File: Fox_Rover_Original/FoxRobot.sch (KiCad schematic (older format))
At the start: 42 parts, among them J1 Screw_Terminal_01x02, J2 XT60-M_Green, J3 XT60-M_Red, J4 Screw_Terminal_01x02, J5 Conn_02x10_Odd_Even, J6 Screw_Terminal_01x02, J7 Conn_02x10_Odd_Even, K1 40.52.7.012.0000, K2 G2RK-1_12DC, K3 ADJH23005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

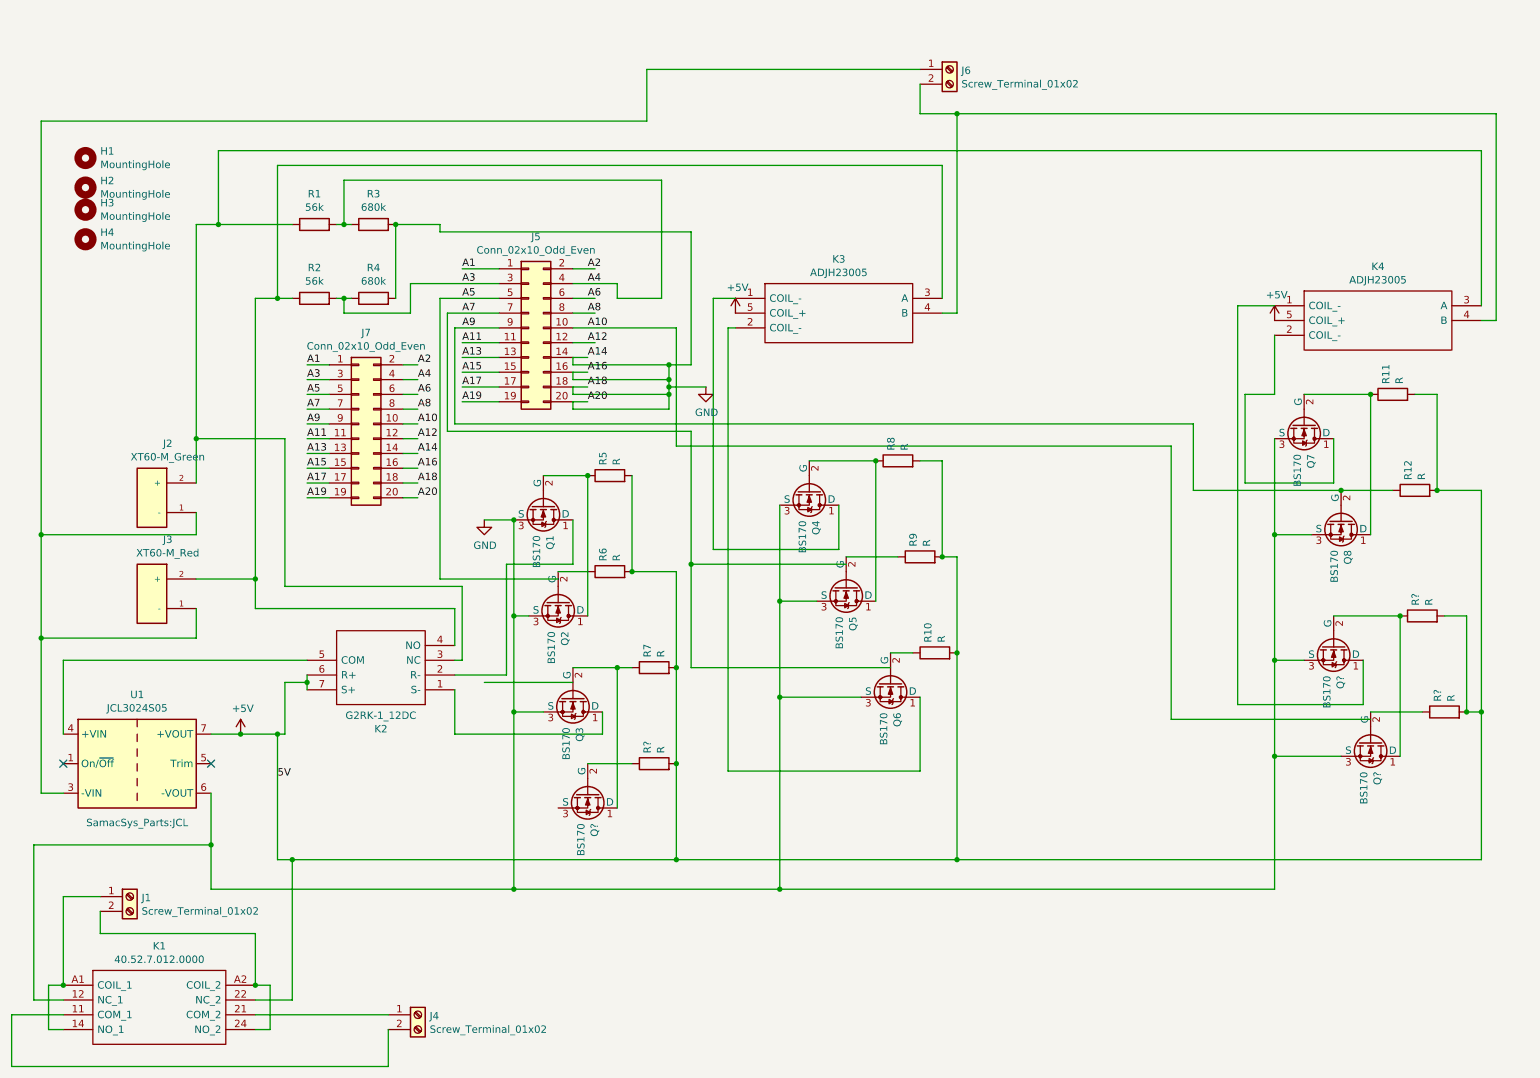
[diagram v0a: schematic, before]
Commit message: Added the filter capacitor and coil.
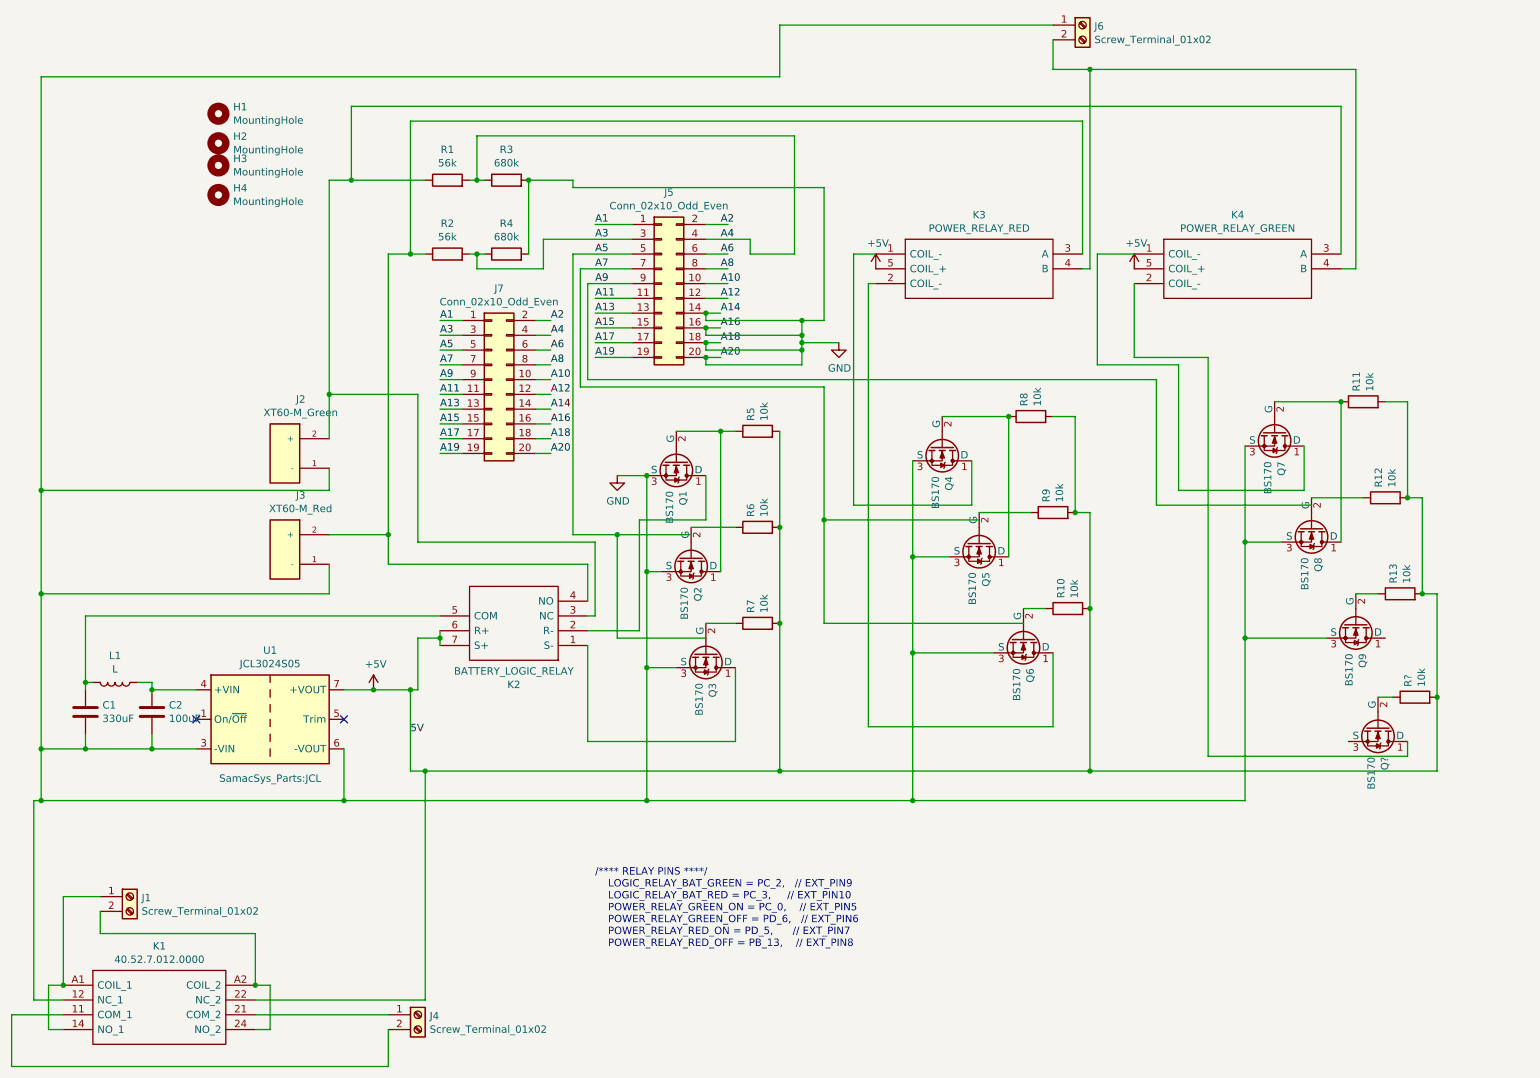
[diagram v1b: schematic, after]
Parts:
- removed Q? (x3): BS170, Package_TO_SOT_THT:TO-92_Inline, symbol Transistor_FET:BS170
- removed R? (x3): R, Resistor_THT:R_Axial_DIN0207_L6.3mm_D2.5mm_P10.16mm_Horizontal, symbol Device:R
- added C1: 330uF, Capacitor_THT:C_Disc_D7.5mm_W2.5mm_P5.00mm, symbol Device:C
- added C2: 100uF, Capacitor_THT:C_Disc_D7.5mm_W2.5mm_P5.00mm, symbol Device:C
- added L1: L, Inductor_THT:L_Radial_D10.0mm_P5.00mm_Fastron_07M, symbol Device:L
- added Q9, Q?: BS170, Package_TO_SOT_THT:TO-92_Inline, symbol Transistor_FET:BS170
- added R13, R?: 10k, Resistor_THT:R_Axial_DIN0207_L6.3mm_D2.5mm_P10.16mm_Horizontal, symbol Device:R
- K2: value G2RK-1_12DC -> BATTERY_LOGIC_RELAY
- K3: value ADJH23005 -> POWER_RELAY_RED
- K4: value ADJH23005 -> POWER_RELAY_GREEN
- R10, R11, R12, R5, R6, R7, R8, R9: value R -> 10k
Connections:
- wire segments 245 -> 247
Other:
- note added: "/**** RELAY PINS ****/\n LOGIC_RELAY_BAT_GREEN = PC_2, // EXT_PIN9\n LOGIC_RELAY_BAT_RED = PC_3, // EXT_PIN10\n POWER_RELAY_GREEN_ON = PC_0, // EXT_PIN5\n POWER_RELAY_GREEN_OFF = PD_6, // EXT_PIN6\n POWER_RELAY_RED_ON = PD_5, // EXT_PIN7\n POWER_RELAY_RED_OFF = PB_13, // EXT_PIN8"
- moved on the sheet: H1, H2, H3, H4, J2, J3, J5, J6, J7, K2, K3, K4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

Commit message: Adjusted libraries pathing
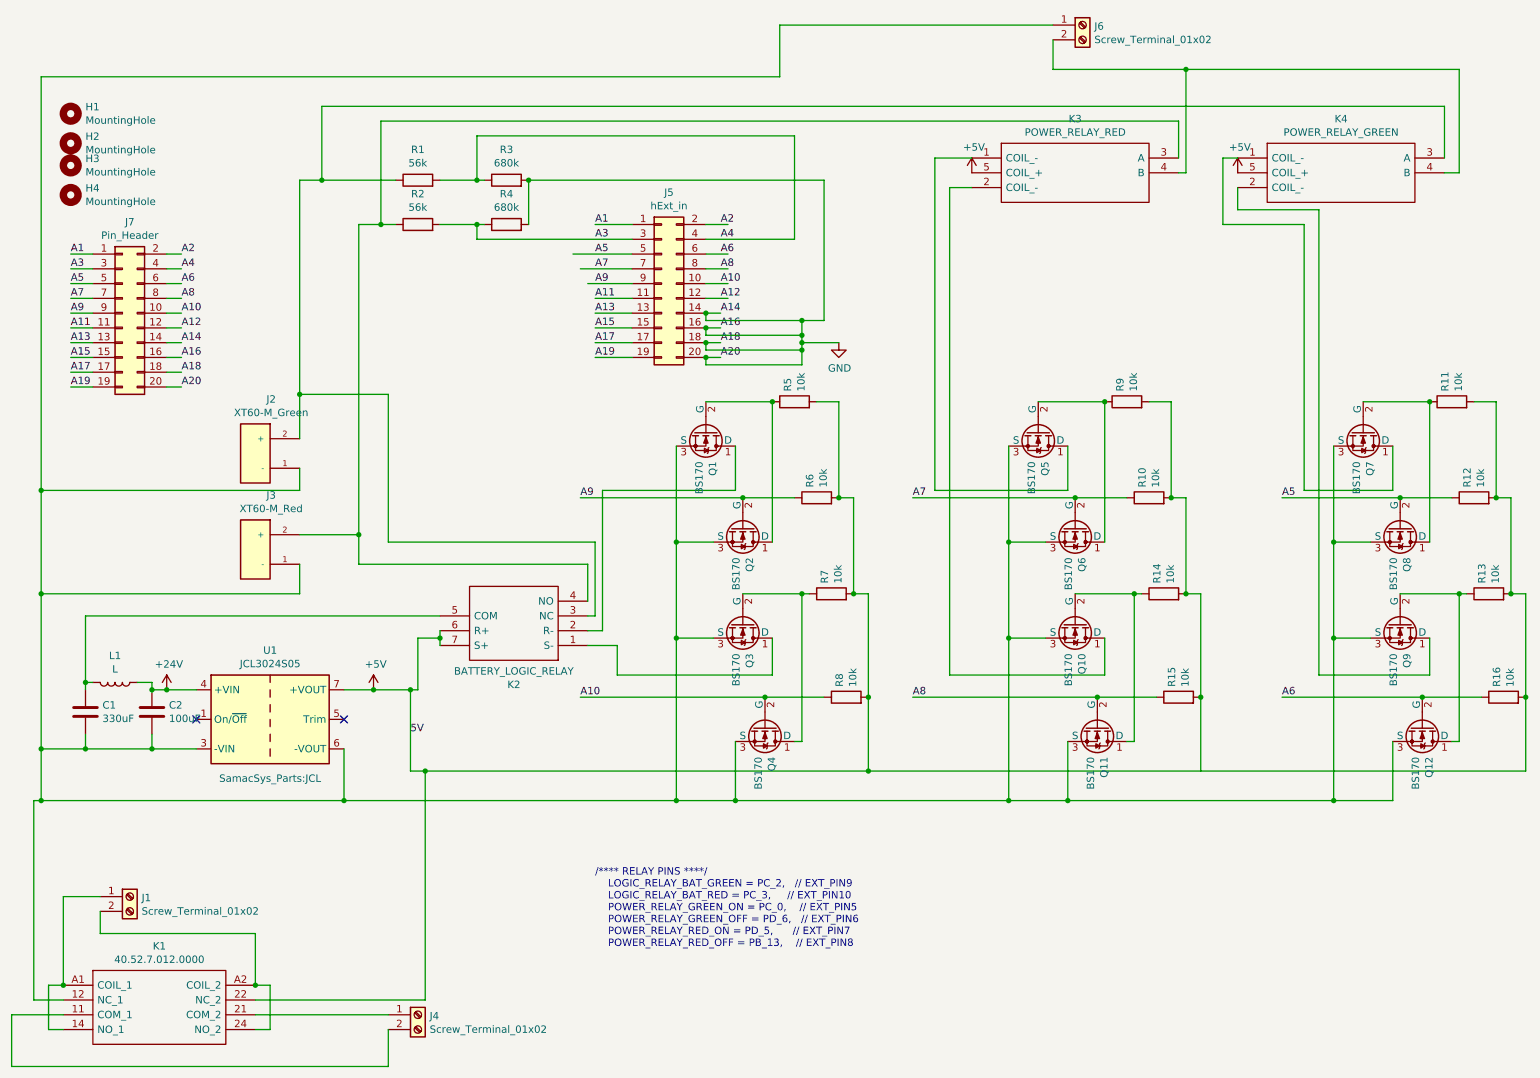
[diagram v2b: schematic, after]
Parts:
- added Q10, Q11: BS170, Package_TO_SOT_THT:TO-92_Inline, symbol Transistor_FET:BS170
- added R14, R15: 10k, Resistor_THT:R_Axial_DIN0207_L6.3mm_D2.5mm_P10.16mm_Horizontal, symbol Device:R
- J5: value Conn_02x10_Odd_Even -> hExt_in
- J7: value Conn_02x10_Odd_Even -> Pin_Header
- gave numbers to parts that had none: 2
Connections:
- net labels added: +24V
- wire segments 247 -> 254
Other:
- moved on the sheet: H1, H2, H3, H4, J2, J3, J7, K3, K4, Q12, Q7, Q8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
